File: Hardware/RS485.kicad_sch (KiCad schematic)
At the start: 18 parts, among them J5 Conn_01x02_Male, J6 Screw_Terminal_01x02, U9 SP3485EN

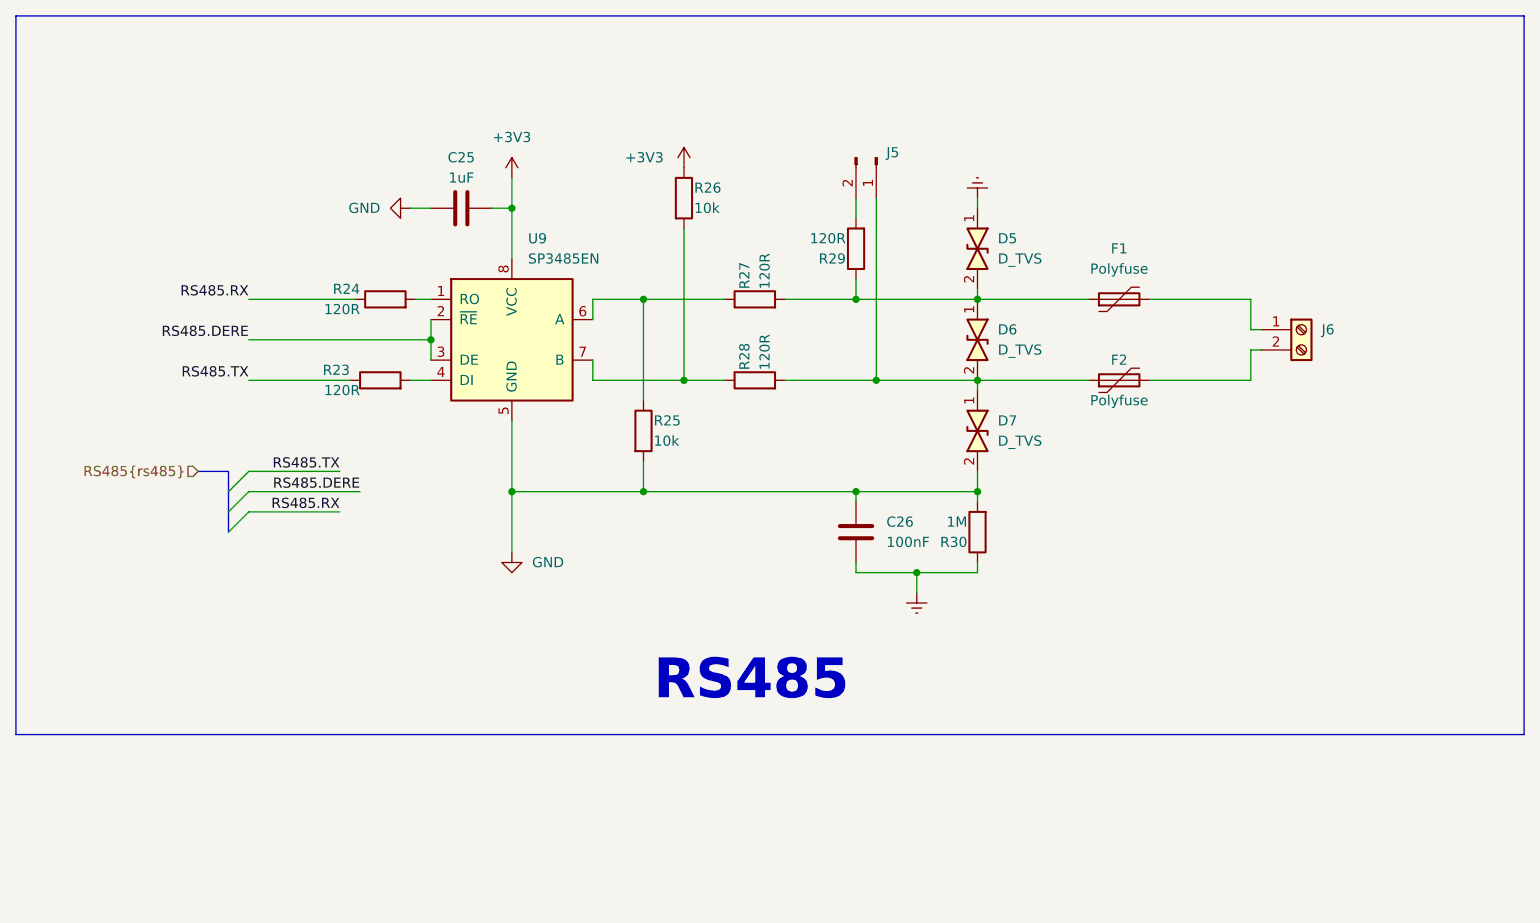
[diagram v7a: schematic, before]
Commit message: Change footprint of MCP41010 and 32.768 crystal
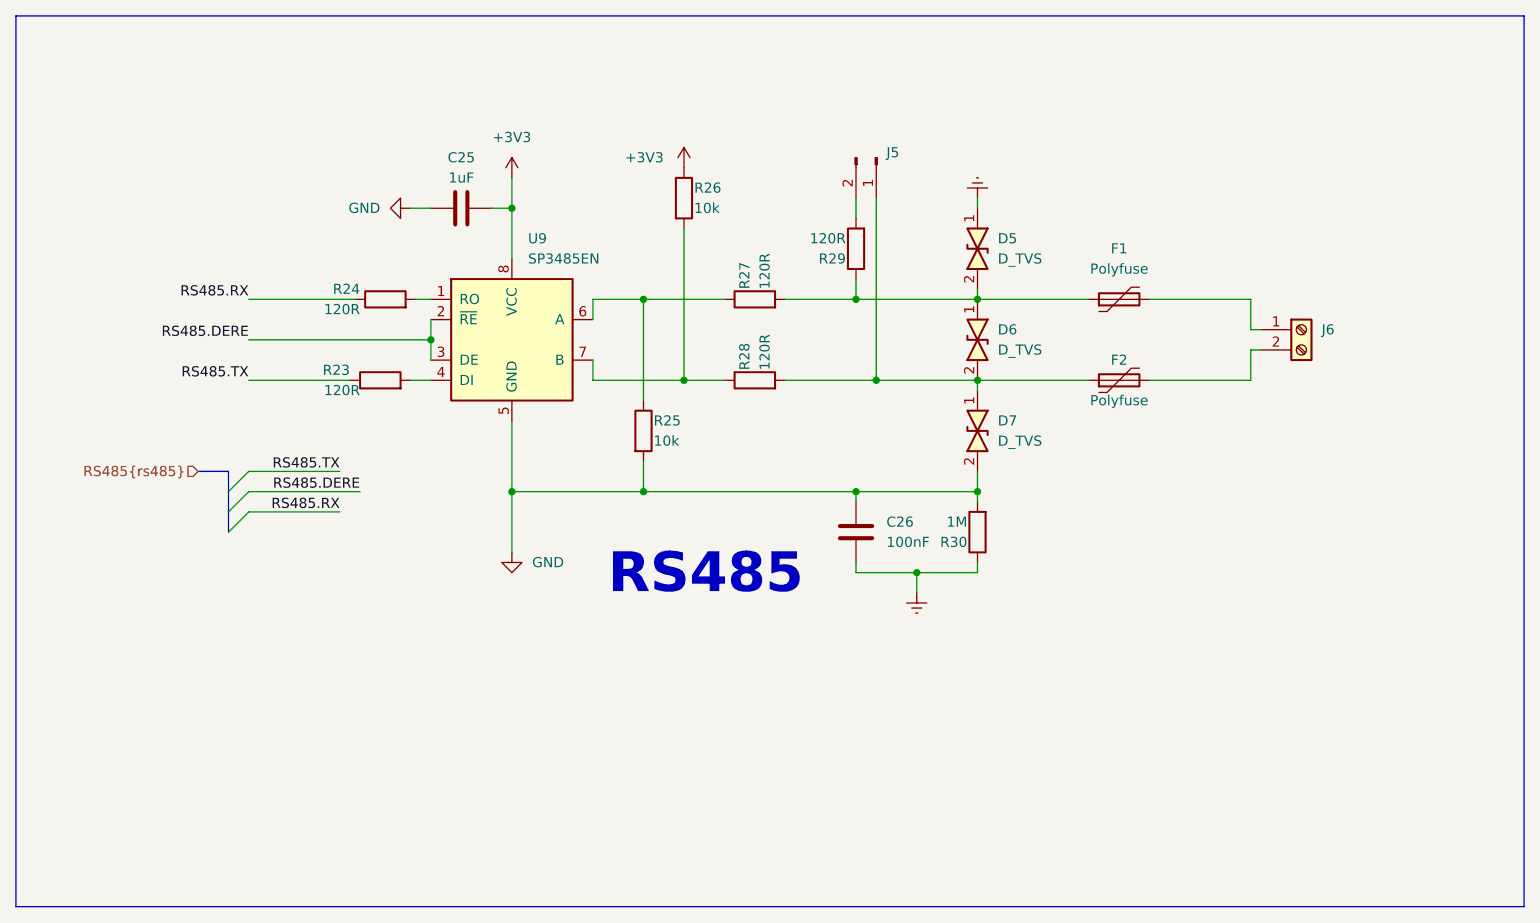
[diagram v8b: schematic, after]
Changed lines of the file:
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@@
     (stroke (width 0) (type default) (color 0 0 0 0))
   )
-  (polyline (pts (xy 46.99 129.54) (xy 236.22 129.54))
+  (polyline (pts (xy 46.99 151.13) (xy 236.22 151.13))
     (stroke (width 0) (type default) (color 0 0 0 0))
   )
@@
     (stroke (width 0) (type default) (color 0 0 0 0))
   )
-  (polyline (pts (xy 46.99 39.37) (xy 46.99 129.54))
+  (polyline (pts (xy 46.99 39.37) (xy 46.99 151.13))
     (stroke (width 0) (type default) (color 0 0 0 0))
   )
@@
     (stroke (width 0) (type default) (color 0 0 0 0))
   )
-  (polyline (pts (xy 236.22 129.54) (xy 236.22 39.37))
+  (polyline (pts (xy 236.22 151.13) (xy 236.22 39.37))
     (stroke (width 0) (type default) (color 0 0 0 0))
   )
@@
     (stroke (width 0) (type default) (color 0 0 0 0))
   )
-  (text "RS485" (at 127 125.73 0)
+  (text "RS485" (at 121.285 112.395 0)
     (effects (font (size 5 5) bold) (justify left bottom))
   )
